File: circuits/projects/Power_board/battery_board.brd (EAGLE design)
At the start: 160 x 100 mm, 31 parts, among them M1-FUSE 3A, M2-FUSE 3A

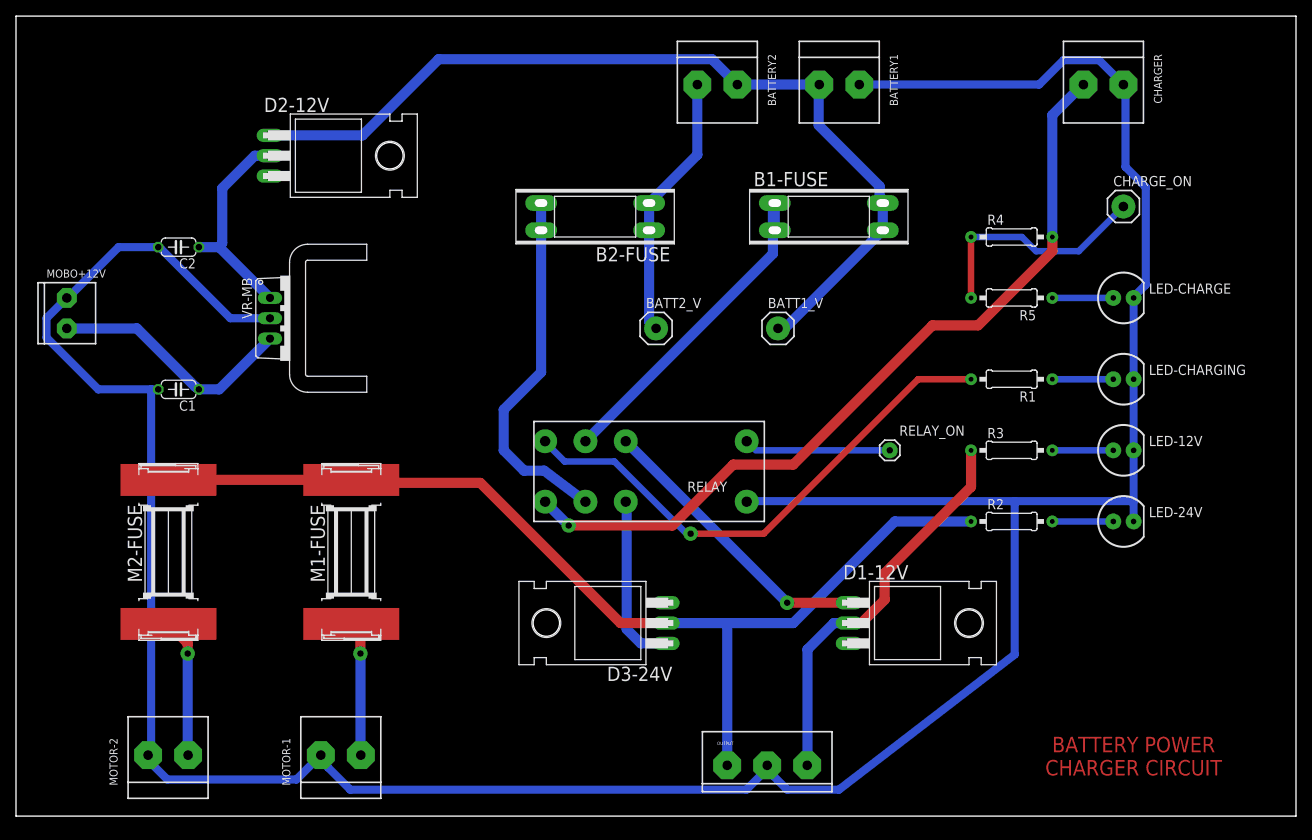
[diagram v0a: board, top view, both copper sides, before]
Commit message: battery board made
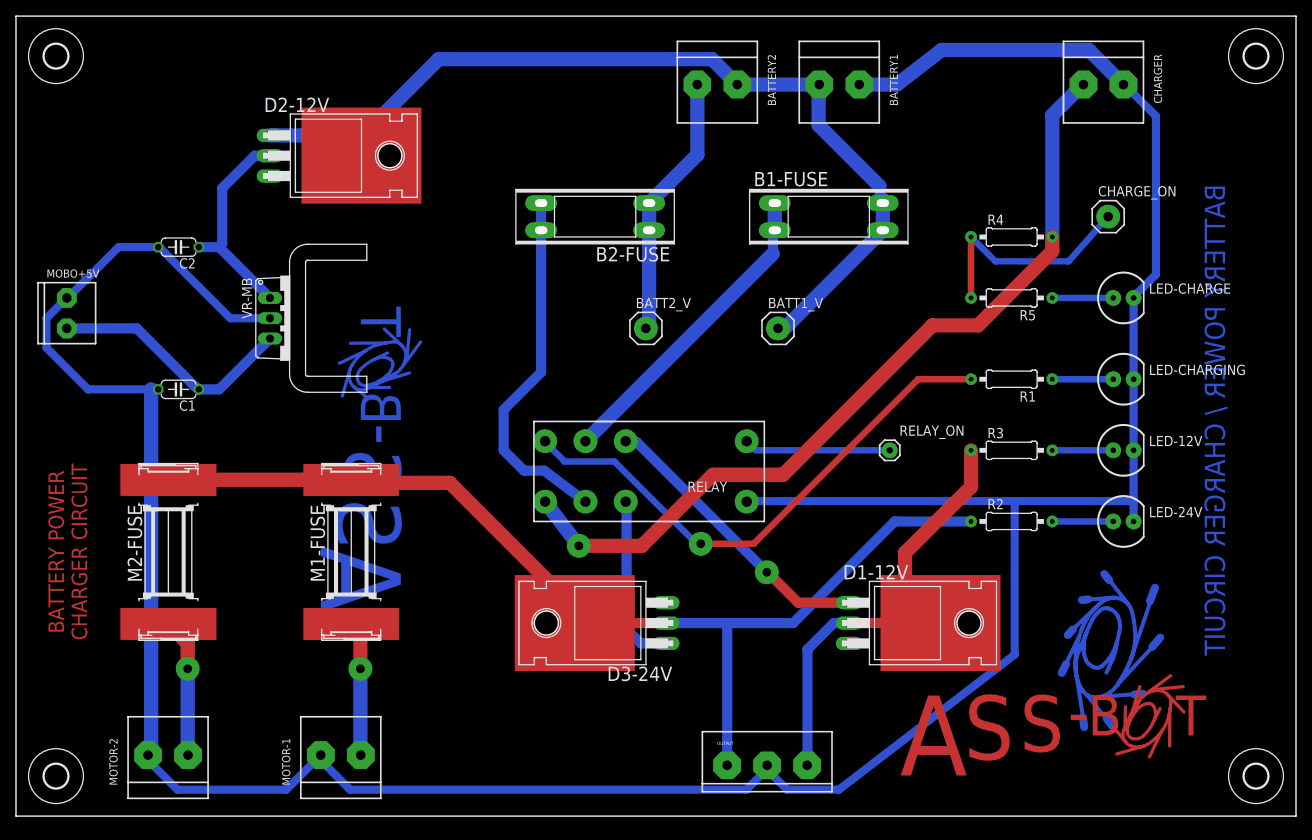
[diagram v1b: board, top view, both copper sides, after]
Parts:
- added U$1, U$7: (no value), parts:LOGO-ASSBOT
- added U$3, U$4, U$5, U$6: (no value), parts:3,0
- added U$8: (no value), parts:LOGO-SYNCHROTRON
- added U$9: (no value), parts:LOGO-SYNCHROTRON-SILK
- moved CHARGE_ON 2.29 mm to (136.5, 74.9)
- moved BATT2_V 1.27 mm to (78.7, 61.0)
- renumbered MOBO+12V to MOBO+5V
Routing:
- net GND: track 381.5 -> 385.6 mm
- net N$2: track 101.3 -> 103.9 mm
- net 12V: track 49.9 -> 51.4 mm
- net N$15: track 29.7 -> 28.5 mm
- net N$13: track 66.1 -> 67.1 mm
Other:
- board text added: "12V"
- board text added: "12V ON"
- board text added: "24V"
- board text added: "24V ON"
- board text added: "5V"
- board text added: "B1"
- board text added: "B1 FUSE"
- board text added: "B2"
- board text added: "B2 FUSE"
- board text added: "BATTERY 1 VOLTAGE"
- board text added: "BATTERY 2 VOLTAGE"
- board text added: "BATTERY POWER / CHARGER CIRCUIT"
- board text added: "CHARGE CONNECTED"
- board text added: "CHARGE ON"
- board text added: "CHARGING"
- board text added: "DRIVE MOTORS"
- board text added: "GND"
- board text added: "M1 FUSE"
- board text added: "M2 FUSE"
- board text added: "MOBO"
- board text added: "OUTPUT"
- board text added: "RELAY ON"
- board text added: "Vin"

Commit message: gittin the night away
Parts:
- moved CHARGER 12.7 mm to (125.7, 91.4)
- moved U$7 10.2 mm to (47.0, 30.5)
- moved U$4 10.0 mm to (145.0, 95.0)
- moved U$5 10.0 mm to (145.0, 5.00)
- moved LED-12V 7.62 mm to (130.8, 45.7)
- moved LED-24V 7.62 mm to (130.8, 36.8)
- moved LED-CHARGE 7.62 mm to (130.8, 64.8)
- moved LED-CHARGING 7.62 mm to (130.8, 54.6)
- moved U$1 5.08 mm to (105.4, 5.08)
- moved CHARGE_ON 3.81 mm to (132.7, 74.9)
- moved R1 3.81 mm to (120.7, 54.6)
- moved R2 3.81 mm to (120.7, 36.8)
- moved R3 3.81 mm to (120.7, 45.7)
- moved R4 3.81 mm to (120.7, 72.4)
- moved R5 3.81 mm to (120.7, 64.8)
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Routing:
- net GND: track 385.6 -> 350.1 mm
- net N$2: track 103.9 -> 118.2 mm
- net N$7: track 7.62 -> 3.81 mm
- net N$3: track 7.62 -> 3.81 mm
- net N$16: track 7.62 -> 3.81 mm
- net N$14: track 7.62 -> 3.81 mm
- net N$13: track 67.1 -> 63.6 mm
- net N$15: track 28.5 -> 25.8 mm
- net 12V: track 51.4 -> 50.1 mm
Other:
- board size 160 x 100 mm -> 150 x 100 mm
- board text added: "Design & Production S. Martin"

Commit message: first board finished
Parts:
- removed B1-FUSE, B2-FUSE: 20A, parts:FUSE_BLADE
- removed M1-FUSE, M2-FUSE: 3A, parts:FUSE-5X20MM_SMD
- added D1: BZX55, parts:DO35Z10
- added FUSE-M1, FUSE-M2: 3A, parts:SCREWTERMINAL-5MM-2
- added U$2: (no value), parts:LOGO-ASSBOT-SILK
- R1, R2, R3, R4, R5: device parts:0207/10 -> parts:0309/15
- RELAY_ON: value 1-HOLE" -> 1-HOLE; device parts:1-HOLE -> parts:1-HOLE_BIG
- moved U$1 96.2 mm to (16.5, 41.9)
- moved U$9 86.2 mm to (95.9, 55.9)
- moved RELAY_ON 33.1 mm to (82.5, 65.4)
- moved BATT2_V 26.2 mm to (62.2, 81.3)
- moved BATT1_V 24.0 mm to (82.5, 81.3)
- moved D1-12V 19.7 mm to (92.7, 29.2)
- moved RELAY 15.5 mm to (69.8, 55.9)
- moved BATTERY2 12.7 mm to (77.5, 91.4)
- moved U$7 12.6 mm to (37.5, 38.7)
- moved D3-24V 11.4 mm to (63.5, 29.2), turned to 270 degrees
- moved MOTOR-1 8.89 mm to (47.0, 7.62)
- moved MOTOR-2 7.62 mm to (24.1, 7.62)
- moved U$8 6.63 mm to (130.2, 15.2)
- moved BATTERY1 6.35 mm to (99.1, 91.4)
- moved C1 4.26 mm to (22.2, 57.1)
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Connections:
- removed net N$20: B2-FUSE.P$2, RELAY.21
- removed net N$39: B1-FUSE.P$1, RELAY.11
- net 24V: now also FUSE-M1.2, FUSE-M2.2; no longer M1-FUSE.P$2, M2-FUSE.P$2
- net GND: now also D1.A
- net N$1: now also RELAY.11; no longer B1-FUSE.P$2
- net N$10: now also FUSE-M1.1, MOTOR-1.2; no longer M2-FUSE.P$1, MOTOR-2.2
- net N$11: now also RELAY_ON.P$1; no longer RELAY_ON.1
- net N$15: now also D1.C
- net N$5: now also RELAY.21; no longer B2-FUSE.P$1
- net N$9: now also FUSE-M2.1, MOTOR-2.2; no longer M1-FUSE.P$1, MOTOR-1.2
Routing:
- net GND: track 350.1 -> 406.4 mm
- net N$20: track 45.4 -> 0.00 mm
- net N$10: track 17.4 -> 61.7 mm, vias 1 -> 2
- net N$39: track 43.4 -> 0.00 mm
- net N$9: track 16.9 -> 47.5 mm, vias 1 -> 2
- net 12V: track 50.1 -> 78.6 mm
- net N$13: track 63.6 -> 90.8 mm
- net N$2: track 118.2 -> 91.5 mm
- net N$5: track 33.1 -> 54.5 mm
- net 24V: track 131.2 -> 145.1 mm
- net N$11: track 18.4 -> 5.89 mm
- net N$15: track 25.8 -> 30.7 mm
- net N$4: track 21.7 -> 25.2 mm
- net N$12: track 26.7 -> 29.7 mm
- net N$1: track 113.7 -> 111.5 mm
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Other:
- board text added: "+12V"
- board text added: "+24V"
- board text added: "CHARGER"
- board text added: "MOTOR 1"
- board text added: "MOTOR 2"
- board text removed: "B1 FUSE"
- board text removed: "B2 FUSE"
- board text removed: "DRIVE MOTORS"

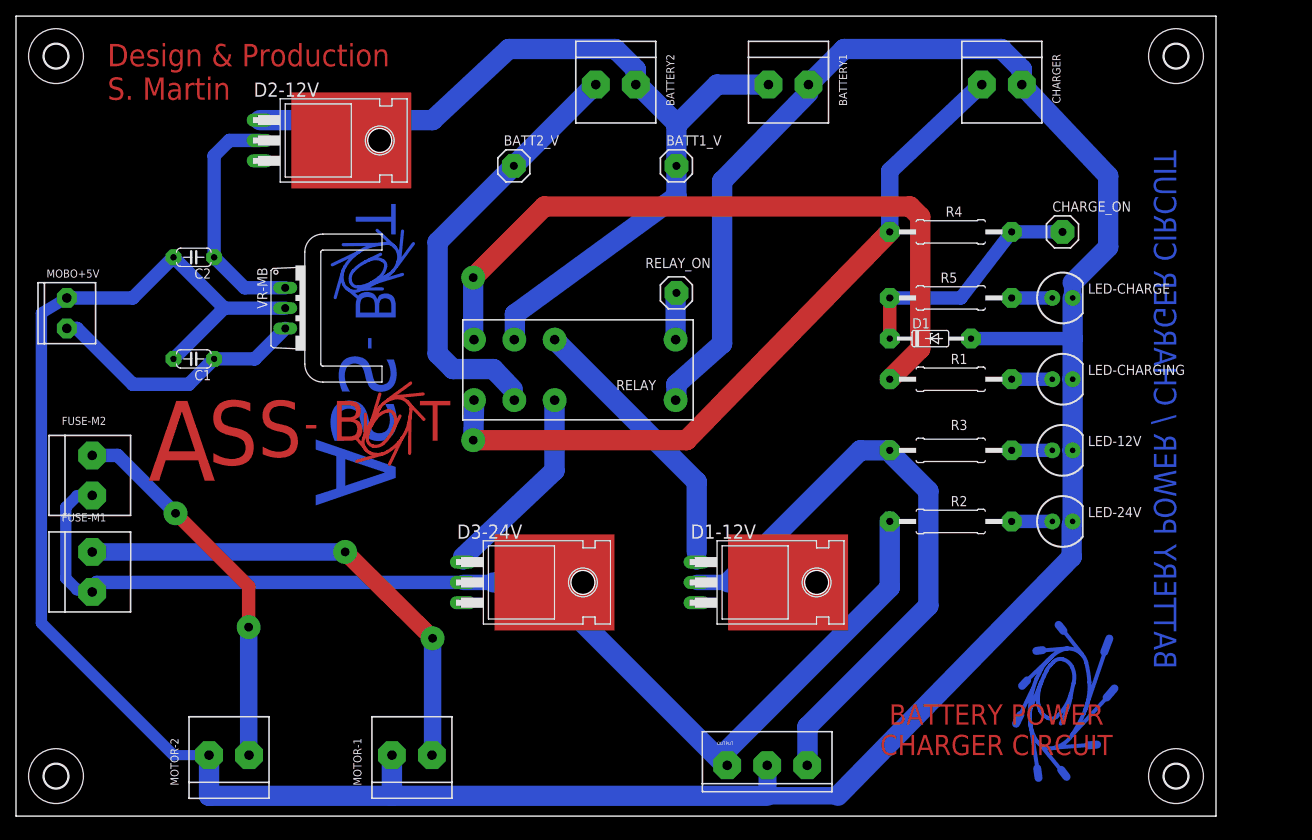
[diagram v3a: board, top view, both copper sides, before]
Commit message: made board tracks bigger
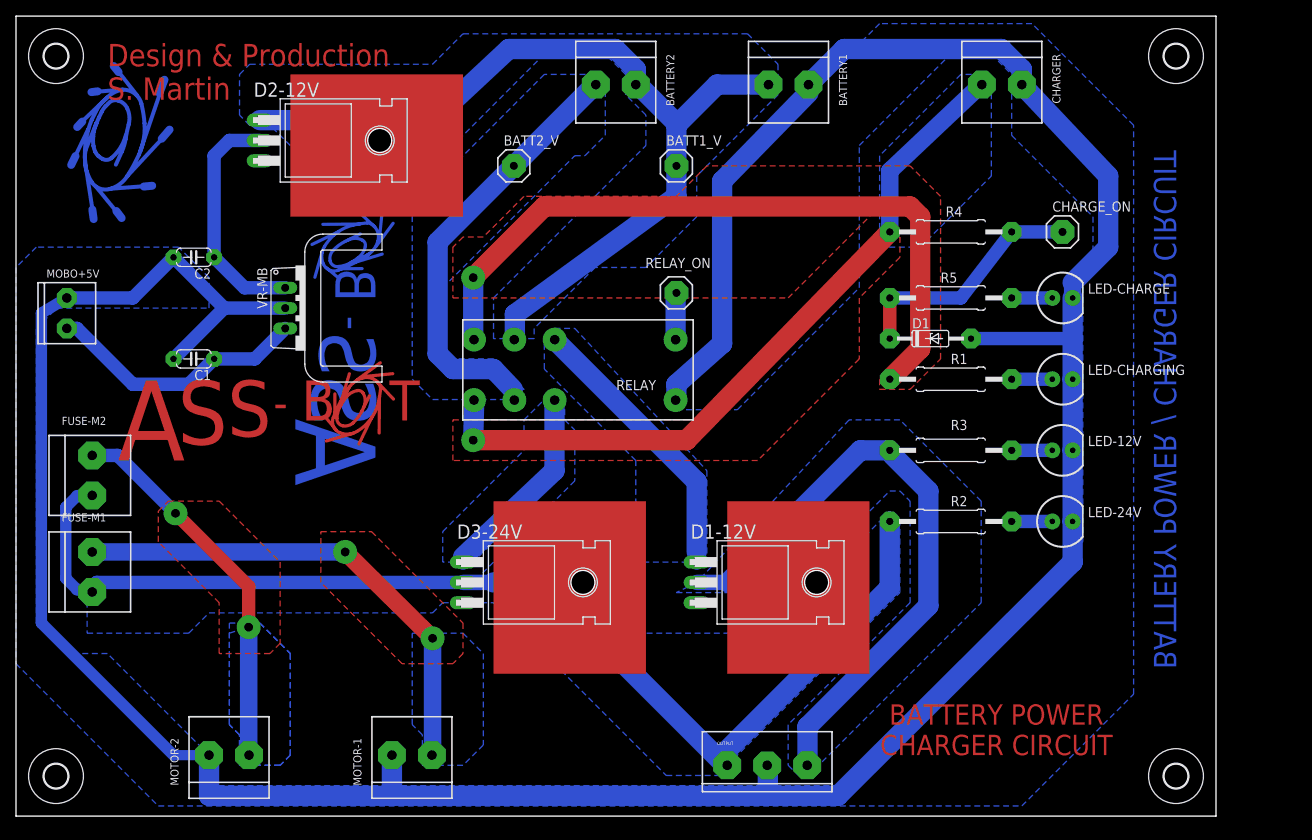
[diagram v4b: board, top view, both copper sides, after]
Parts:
- moved U$8 137.2 mm to (12.1, 85.1)
- moved U$1 4.58 mm to (12.7, 44.5)
- moved U$7 3.59 mm to (34.9, 41.3)
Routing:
- added copper zone on layer 16, net 12V
- added copper zone on layer 16, net 24V
- added copper zone on layer 16, net GND
- added copper zone on layer 16, net N$1
- added copper zone on layer 1, net N$10
- added copper zone on layer 16, net N$10
- added copper zone on layer 1, net N$13
- added copper zone on layer 1, net N$2
- added copper zone on layer 16, net N$2
- added copper zone on layer 16, net N$4
- added copper zone on layer 16, net N$5
- added copper zone on layer 16, net N$6
- added copper zone on layer 1, net N$9
- added copper zone on layer 16, net N$9

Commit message: new shit
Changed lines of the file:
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@@
 <setting verticaltext="up"/>
 </settings>
-<grid distance="0.05" unitdist="inch" unit="inch" style="lines" multiple="1" display="yes" altdistance="0.025" altunitdist="inch" altunit="inch"/>
+<grid distance="25" unitdist="mil" unit="mil" style="lines" multiple="1" display="yes" altdistance="12.5" altunitdist="inch" altunit="inch"/>
 <layers>
 <layer number="1" name="Top" color="4" fill="1" visible="yes" active="yes"/>
@@
 </class>
 </classes>
-<designrules name="rules">
+<designrules name="rules *">
 <description language="de">&lt;b&gt;EAGLE Design Rules&lt;/b&gt;
 &lt;p&gt;
@@
 <param name="srMinRoundness" value="0mil"/>
 <param name="srMaxRoundness" value="0mil"/>
-<param name="slThermalIsolate" value="10mil"/>
-<param name="slThermalsForVias" value="0"/>
+<param name="slThermalIsolate" value="0mil"/>
+<param name="slThermalsForVias" value="1"/>
 <param name="dpMaxLengthDifference" value="10mm"/>
 <param name="dpGapFactor" value="2.5"/>
@@
 <wire x1="93.98" y1="91.44" x2="87.63" y2="91.44" width="2.54" layer="16"/>
 <wire x1="87.63" y1="91.44" x2="82.55" y2="86.36" width="2.54" layer="16"/>
-<wire x1="30.48" y1="86.995" x2="52.07" y2="86.995" width="2.54" layer="16"/>
-<wire x1="52.07" y1="86.995" x2="61.595" y2="95.885" width="2.54" layer="16"/>
+<wire x1="30.48" y1="86.995" x2="31.75" y2="86.995" width="2.54" layer="16"/>
+<wire x1="31.75" y1="86.995" x2="33.02" y2="88.265" width="2.54" layer="16"/>
+<wire x1="33.02" y1="88.265" x2="53.975" y2="88.265" width="2.54" layer="16"/>
+<wire x1="53.975" y1="88.265" x2="61.595" y2="95.885" width="2.54" layer="16"/>
 <wire x1="61.595" y1="95.885" x2="74.93" y2="95.885" width="2.54" layer="16"/>
 <wire x1="74.93" y1="95.885" x2="77.47" y2="93.345" width="2.54" layer="16"/>
@@
 <wire x1="120.65" y1="91.44" x2="109.22" y2="80.645" width="2.1844" layer="16"/>
 <wire x1="120.65" y1="91.44" x2="120.73" y2="91.44" width="1.524" layer="16"/>
-<wire x1="57.15" y1="46.99" x2="57.277" y2="51.943" width="2.54" layer="16"/>
+<wire x1="57.15" y1="46.99" x2="57.277" y2="51.943" width="3.81" layer="16"/>
 <wire x1="57.277" y1="51.943" x2="57.25" y2="52" width="1.524" layer="16"/>
 <via x="57.15" y="46.99" extent="1-16" drill="1.1" diameter="3"/>
@@
 <contactref element="RELAY_ON" pad="P$1"/>
 <contactref element="RELAY" pad="A1"/>
-<wire x1="82.45" y1="59.56" x2="82.45" y2="65.305" width="2.54" layer="16"/>
+<wire x1="82.45" y1="59.56" x2="82.45" y2="65.305" width="3.81" layer="16"/>
 <wire x1="82.45" y1="65.305" x2="82.55" y2="65.405" width="0.8128" layer="16"/>
 </signal>
@@
 <via x="57.15" y="67.31" extent="1-16" drill="1.1" diameter="3"/>
 <wire x1="57.785" y1="59.69" x2="57.15" y2="59.69" width="0.8128" layer="16"/>
-<wire x1="57.15" y1="59.69" x2="57.15" y2="67.31" width="2.54" layer="16"/>
+<wire x1="57.15" y1="59.69" x2="57.15" y2="67.31" width="3.81" layer="16"/>
 <wire x1="57.15" y1="67.31" x2="66.04" y2="76.2" width="2.54" layer="1"/>
 <wire x1="66.04" y1="76.2" x2="111.76" y2="76.2" width="2.54" layer="1"/>

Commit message: new boards
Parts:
- removed BATT1_V, BATT2_V, CHARGE_ON, RELAY_ON: 1-HOLE, parts:1-HOLE_BIG
- removed C1: 10uF, parts:C050-024X044
- removed C2: 2.2uF, parts:C050-024X044
- removed CHARGER: 24V, parts:SCREWTERMINAL-5MM-2
- removed D1: BZX55, parts:DO35Z10
- removed D2-12V: 30A, parts:TO22-DIODE-H
- removed LED-CHARGE, LED-CHARGING: (no value), parts:LED5MM
- removed MOBO+5V: 2-HOLESSC3.81MM, parts:SCREWTERMINAL-3.81MM
- removed R1: 560R, parts:0309/15
- removed R4: 1k, parts:0309/15
- removed R5: 220R, parts:0309/15
- removed RELAY: 5V, parts:RELAY_RT2
- removed U$9: (no value), parts:LOGO-SYNCHROTRON-SILK
- removed VR-MB: LT323A, parts:TO220V-HEATSINK
- added +5V-1, +5V-2, +5V-3: 2-HOLESSC3.81MM, parts:SCREWTERMINAL-3.81MM
- added C1_V1, C1_V2, C1_V3: 2.2uF, parts:C050-024X044
- added C2_V1, C2_V2, C2_V3: 10uF, parts:C050-024X044
- added OUTPUT-SHAFT: 3-HOLE, parts:SCREWTERMINAL-5MM-3@1
- added TEST: (no value), parts:1X03
- added U$10: (no value), parts:LOGO-SYNCHROTRON-SILK
- added VR-MB1, VR-MB2, VR-MB3: LT323A, parts:TO220V-HEATSINK2
- OUTPUT: device parts:SCREWTERMINAL-5MM-3 -> parts:SCREWTERMINAL-5MM-3@1
- U$1: device parts:LOGO-ASSBOT -> parts:LOGO-SYNCHROTRON
- moved U$1 114.6 mm to (127.3, 43.5)
- moved U$8 102.2 mm to (105.4, 43.5), turned to 0 degrees
- moved OUTPUT 95.3 mm to (129.2, 92.7), turned to 180 degrees
- moved MOTOR-1 75.7 mm to (7.30, 72.1), turned to 270 degrees
- moved U$2 70.5 mm to (40.6, 40.0)
- moved FUSE-M1 61.8 mm to (24.1, 93.0), turned to 180 degrees
- moved FUSE-M2 57.2 mm to (40.6, 93.0), turned to 180 degrees
- moved MOTOR-2 49.4 mm to (6.99, 54.0), turned to 270 degrees
- moved D3-24V 40.5 mm to (60.0, 69.5), turned to 180 degrees
- moved D1-12V 27.6 mm to (93.7, 56.8)
- moved U$7 25.5 mm to (42.2, 16.8), turned to 0 degrees
- moved R2 19.9 mm to (124.5, 55.2)
- moved LED-24V 19.6 mm to (137.5, 55.2)
- moved R3 19.1 mm to (124.5, 63.2)
- moved LED-12V 18.7 mm to (137.5, 63.2)
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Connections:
- removed net N$11: RELAY.A1, RELAY_ON.P$1
- removed net N$12: C2.1, D2-12V.P$2, VR-MB.1
- removed net N$13: R1.2, RELAY.14
- removed net N$16: LED-CHARGE.A, R5.1
- removed net N$2: CHARGER.2, R4.2, RELAY.24
- removed net N$5: BATT2_V.P$1, BATTERY2.2, RELAY.21
- removed net N$6: D1-12V.P$1, RELAY.12
- removed net N$7: LED-CHARGING.A, R1.1
- new net N$17: +5V-1.2, C2_V1.1, VR-MB1.3
- net 12V: now also C1_V1.1, C1_V2.1, C1_V3.1, OUTPUT-SHAFT.3, VR-MB1.1, VR-MB2.1, VR-MB3.1
- net 24V: now also OUTPUT-SHAFT.1
- net GND: now also +5V-1.1, +5V-2.1, +5V-3.1, C1_V1.2, C1_V2.2, C1_V3.2, C2_V1.2, C2_V2.2, C2_V3.2, OUTPUT-SHAFT.2, TEST.1, VR-MB1.2, VR-MB2.2, VR-MB3.2; no longer C1.2, C2.2, CHARGER.1, D1.A, LED-CHARGE.K, LED-CHARGING.K, MOBO+5V.1, RELAY.A2, VR-MB.2
- net N$1: now also D1-12V.P$1, TEST.2; no longer BATT1_V.P$1, D2-12V.P$1, RELAY.11
- net N$15: now also +5V-2.2, C2_V2.1, VR-MB2.3; no longer CHARGE_ON.P$1, D1.C, R4.1, R5.2
- net N$4: now also BATTERY2.2, TEST.3; no longer RELAY.22
- net N$8: now also +5V-3.2, C2_V3.1, VR-MB3.3; no longer C1.1, MOBO+5V.2, VR-MB.3
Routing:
- net 12V: track 78.6 -> 284.9 mm
- net GND: track 406.6 -> 511.3 mm, vias 0 -> 4
- net N$2: track 91.5 -> 0.00 mm, vias 1 -> 0
- net N$13: track 90.8 -> 0.00 mm, vias 1 -> 0
- net 24V: track 145.1 -> 208.3 mm, vias 0 -> 3
- net N$5: track 54.5 -> 0.00 mm
- net N$1: track 111.7 -> 58.0 mm
- net N$6: track 35.2 -> 0.00 mm
- net N$12: track 29.7 -> 0.00 mm
- net N$17: track 0.00 -> 24.9 mm
- net N$9: track 47.5 -> 70.1 mm
- net N$10: track 61.7 -> 44.0 mm
- net N$8: track 33.1 -> 25.0 mm
- net N$4: track 25.2 -> 33.2 mm
- net N$11: track 5.89 -> 0.00 mm
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- added copper zone on layer 1, net MASK
- removed copper zone on layer 16, net 12V
- removed copper zone on layer 16, net 24V
- removed copper zone on layer 16, net N$1
- removed copper zone on layer 1, net N$10
- removed copper zone on layer 16, net N$10
- removed copper zone on layer 1, net N$13
- removed copper zone on layer 1, net N$2
- removed copper zone on layer 16, net N$2
- removed copper zone on layer 16, net N$4
- removed copper zone on layer 16, net N$5
- removed copper zone on layer 16, net N$6
- removed copper zone on layer 1, net N$9
- removed copper zone on layer 16, net N$9
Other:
- board text added: "BATTERY POWER CIRCUIT"
- board text added: "VOLTAGE TEST"
- board text removed: "BATTERY 1 VOLTAGE"
- board text removed: "BATTERY 2 VOLTAGE"
- board text removed: "BATTERY POWER CHARGER CIRCUIT"
- board text removed: "CHARGE CONNECTED"
- board text removed: "CHARGE ON"
- board text removed: "CHARGER"
- board text removed: "CHARGING"
- board text removed: "MOBO"
- board text removed: "RELAY ON"
- board text removed: "Vin"

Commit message: some boards updated
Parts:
- added U$9: (no value), parts:LOGO-ASSBOT
- moved U$1 1.59 mm to (128.9, 43.5)
